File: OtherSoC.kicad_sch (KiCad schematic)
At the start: 1 part, among them U2 rv1126/rv1109

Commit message: replaced Leaf libraries with combined libraries
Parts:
- U2: footprint Rockchip_SoC:Rockchip_RV1126_FCCSP409LD_14.0x14.0mm -> IotPi_Rockchip_SoC:Rockchip_RV1126_FCCSP409LD_14.0x14.0mm
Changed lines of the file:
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@@
       (effects (font (size 1.27 1.27)))
     )
-    (property "Footprint" "Rockchip_SoC:Rockchip_RV1126_FCCSP409LD_14.0x14.0mm" (at 223.52 153.67 0)
+    (property "Footprint" "IotPi_Rockchip_SoC:Rockchip_RV1126_FCCSP409LD_14.0x14.0mm" (at 223.52 153.67 0)
       (effects (font (size 1.27 1.27)) hide)
     )
@@
       (effects (font (size 1.27 1.27)))
     )
-    (property "Footprint" "Rockchip_SoC:Rockchip_RV1126_FCCSP409LD_14.0x14.0mm" (at 99.06 93.98 0)
+    (property "Footprint" "IotPi_Rockchip_SoC:Rockchip_RV1126_FCCSP409LD_14.0x14.0mm" (at 99.06 93.98 0)
       (effects (font (size 1.27 1.27)) hide)
     )
@@
       (effects (font (size 1.27 1.27)))
     )
-    (property "Footprint" "Rockchip_SoC:Rockchip_RV1126_FCCSP409LD_14.0x14.0mm" (at 238.76 96.52 0)
-      (effects (font (size 1.27 1.27)) hide)
-    )
+    (property "Footprint" "IotPi_Rockchip_SoC:Rockchip_RV1126_FCCSP409LD_14.0x14.0mm" (at 238.76 96.52 0)
+      (effects (font (size 1.27 1.27)) hide)
+    )

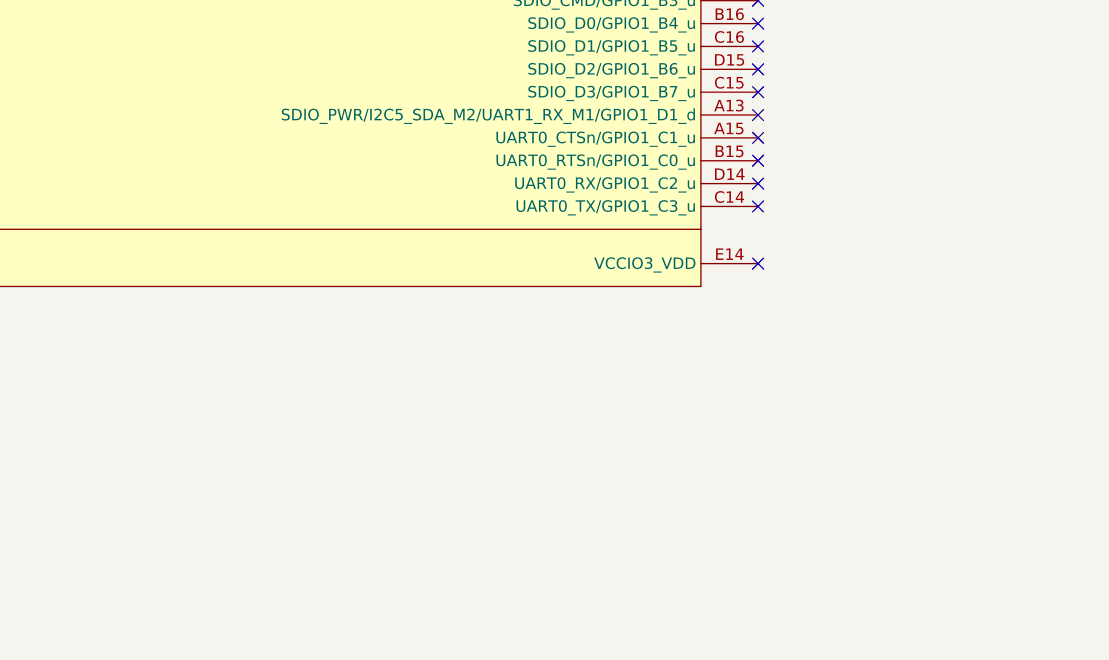
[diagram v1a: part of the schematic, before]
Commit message: updated schematics due to upgrade to 7.99
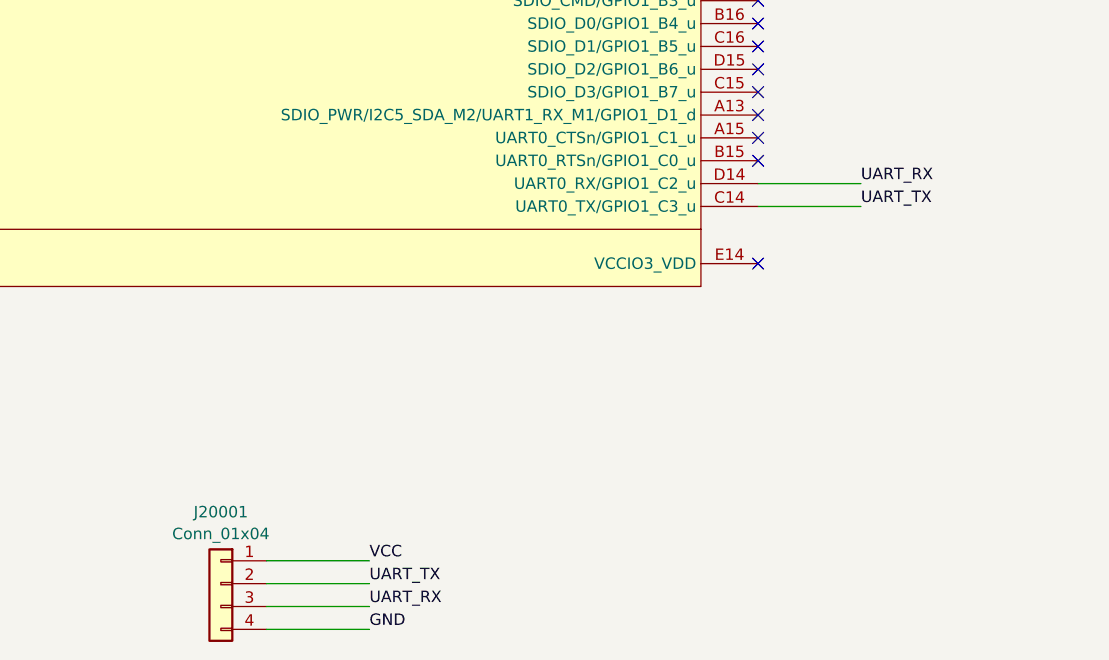
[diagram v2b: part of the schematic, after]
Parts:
- added J20001: Conn_01x04, symbol Connector_Generic:Conn_01x04
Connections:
- net UART_TX: now reaches U2.C14 (UART0_TX/GPIO1_C3_u)
- net UART_TX: now also J20001.2 (Pin_2)
- net UART_RX: now reaches U2.D14 (UART0_RX/GPIO1_C2_u)
- net UART_RX: now also J20001.3 (Pin_3)
- new net GND: J20001.4 (Pin_4)
- new net VCC: J20001.1 (Pin_1)
- no-connect marks 35 -> 33
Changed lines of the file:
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@@
-(kicad_sch (version 20230121) (generator eeschema)
+(kicad_sch (version 20230819) (generator eeschema)
   (paper "A4")
   (title_block
@@
   (no_connect (at 259.08 64.77))
   (no_connect (at 114.3 60.96))
-  (no_connect (at 114.3 76.2))
-  (no_connect (at 114.3 73.66))
   (no_connect (at 114.3 58.42))
   (no_connect (at 114.3 43.18))
@@
   (no_connect (at 114.3 48.26))
   (no_connect (at 259.08 58.42))
+  (wire (pts (xy 59.69 123.19) (xy 71.12 123.19))
+    (stroke (width 0) (type default))
+  )
+  (wire (pts (xy 59.69 120.65) (xy 71.12 120.65))
+    (stroke (width 0) (type default))
+  )
+  (wire (pts (xy 114.3 73.66) (xy 125.73 73.66))
+    (stroke (width 0) (type default))
+  )
+  (wire (pts (xy 114.3 76.2) (xy 125.73 76.2))
+    (stroke (width 0) (type default))
+  )
+  (wire (pts (xy 59.69 118.11) (xy 71.12 118.11))
+    (stroke (width 0) (type default))
+  )
+  (wire (pts (xy 59.69 115.57) (xy 71.12 115.57))
+    (stroke (width 0) (type default))
+  )
+  (label "GND" (at 71.12 123.19 0) (fields_autoplaced)
+    (effects (font (size 1.27 1.27)) (justify left bottom))
+  )
+  (label "UART_TX" (at 71.12 118.11 0) (fields_autoplaced)
+    (effects (font (size 1.27 1.27)) (justify left bottom))
+  )
+  (label "UART_RX" (at 125.73 73.66 0) (fields_autoplaced)
+    (effects (font (size 1.27 1.27)) (justify left bottom))
+  )
+  (label "UART_TX" (at 125.73 76.2 0) (fields_autoplaced)
+    (effects (font (size 1.27 1.27)) (justify left bottom))
+  )
+  (label "UART_RX" (at 71.12 120.65 0) (fields_autoplaced)
+    (effects (font (size 1.27 1.27)) (justify left bottom))
+  )
+  (label "VCC" (at 71.12 115.57 0) (fields_autoplaced)
+    (effects (font (size 1.27 1.27)) (justify left bottom))
+  )
   (symbol (lib_id "IotPi_CPU_Rockchip:rv1126_rv1109") (at 191.77 106.68 0) (unit 13)
-    (in_bom yes) (on_board yes) (dnp no) (fields_autoplaced)
+    (exclude_from_sim no) (in_bom yes) (on_board yes) (dnp no) (fields_autoplaced)
     (property "Reference" "U2" (at 191.77 92.3671 0)
       (effects (font (size 1.27 1.27)))
@@
       (effects (font (size 1.27 1.27)) hide)
     )
+    (property "Description" "" (at 191.77 106.68 0)
+      (effects (font (size 1.27 1.27)) hide)
+    )
     (property "LCSC" "" (at 191.77 106.68 0)
-      (effects (font (size 1.27 1.27)) hide)
-    )
-    (property "Description" "" (at 191.77 106.68 0)
       (effects (font (size 1.27 1.27)) hide)
     )
@@
   )
   (symbol (lib_id "IotPi_CPU_Rockchip:rv1126_rv1109") (at 67.31 46.99 0) (unit 8)
-    (in_bom yes) (on_board yes) (dnp no) (fields_autoplaced)
+    (exclude_from_sim no) (in_bom yes) (on_board yes) (dnp no) (fields_autoplaced)
     (property "Reference" "U2" (at 67.31 27.5971 0)
       (effects (font (size 1.27 1.27)))
@@
       (effects (font (size 1.27 1.27)) hide)
     )
+    (property "Description" "" (at 67.31 46.99 0)
+      (effects (font (size 1.27 1.27)) hide)
+    )
     (property "LCSC" "" (at 67.31 46.99 0)
-      (effects (font (size 1.27 1.27)) hide)
-    )
-    (property "Description" "" (at 67.31 46.99 0)
       (effects (font (size 1.27 1.27)) hide)
     )
@@
   )
   (symbol (lib_id "IotPi_CPU_Rockchip:rv1126_rv1109") (at 207.01 49.53 0) (unit 12)
-    (in_bom yes) (on_board yes) (dnp no) (fields_autoplaced)
+    (exclude_from_sim no) (in_bom yes) (on_board yes) (dnp no) (fields_autoplaced)
     (property "Reference" "U2" (at 207.01 26.3271 0)
       (effects (font (size 1.27 1.27)))
@@
       (effects (font (size 1.27 1.27)) hide)
     )
+    (property "Description" "" (at 207.01 49.53 0)
+      (effects (font (size 1.27 1.27)) hide)
+    )
     (property "LCSC" "" (at 207.01 49.53 0)
-      (effects (font (size 1.27 1.27)) hide)
-    )
-    (property "Description" "" (at 207.01 49.53 0)
       (effects (font (size 1.27 1.27)) hide)
     )
@@
         )
       )
+    )
+  )
+  (symbol (lib_id "Connector_Generic:Conn_01x04") (at 54.61 118.11 0) (mirror y) (unit 1)
+    (exclude_from_sim no) (in_bom yes) (on_board yes) (dnp no) (fields_autoplaced)
+    (property "Reference" "J20001" (at 54.61 110.1555 0)
+      (effects (font (size 1.27 1.27)))
+    )
+    (property "Value" "Conn_01x04" (at 54.61 112.5798 0)
+      (effects (font (size 1.27 1.27)))
+    )
+    (property "Footprint" "" (at 54.61 118.11 0)
+      (effects (font (size 1.27 1.27)) hide)
+    )
+    (property "Datasheet" "~" (at 54.61 118.11 0)
+      (effects (font (size 1.27 1.27)) hide)
+    )
+    (property "Description" "Generic connector, single row, 01x04, script generated (kicad-library-utils/schlib/autogen/connector/)" (at 54.61 118.11 0)
+      (effects (font (size 1.27 1.27)) hide)
+    )
+    (pin "4")
+    (pin "3")
+    (pin "1")
+    (pin "2")
+    (instances
+      (project "leaf"
+        (path "/e3b58043-16a3-43c8-9fad-9c9784eebfa4/56630686-fff3-4c34-8fc7-0dd6f7e78092"
+          (reference "J20001") (unit 1)
+        )
+      )
